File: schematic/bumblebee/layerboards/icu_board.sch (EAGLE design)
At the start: 20 parts, among them P1 B5B-EH-A

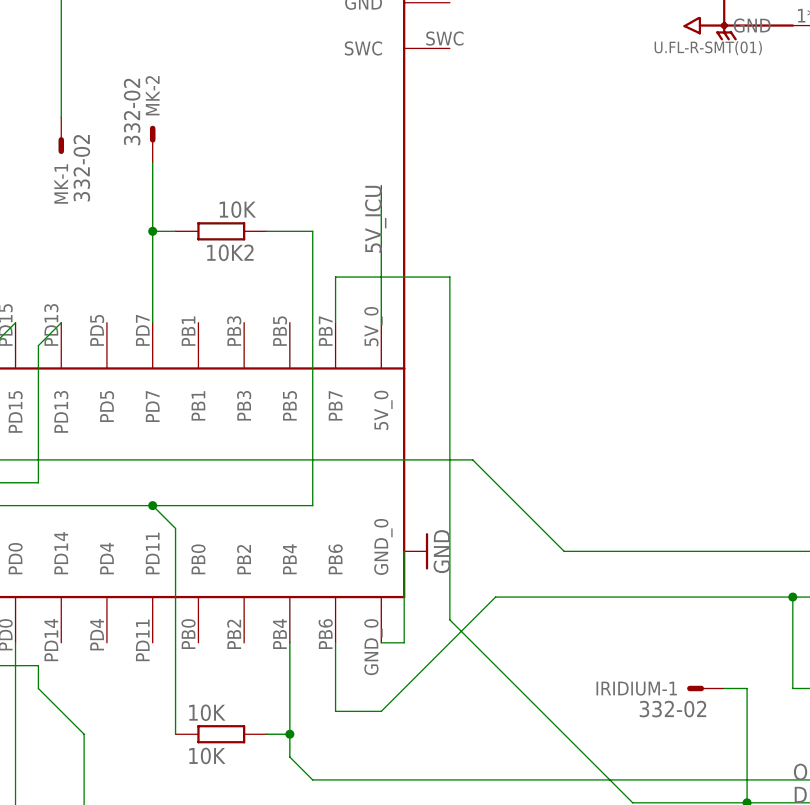
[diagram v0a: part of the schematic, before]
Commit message: CCU и ICU полностью готовы. Было бы здорово, если бы ещё кто-то посмотрел По SCU требуются уточнения
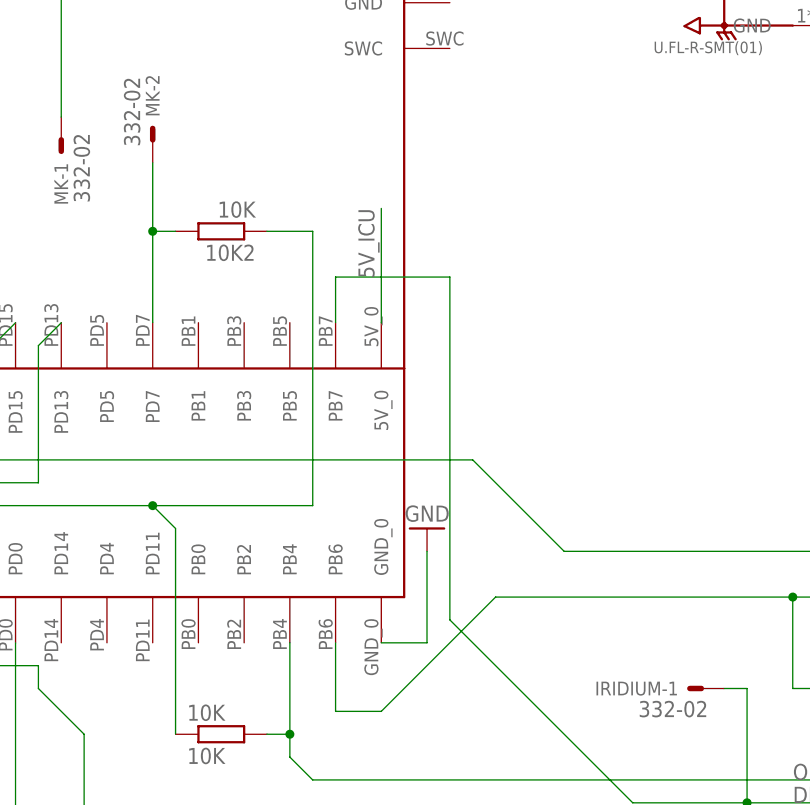
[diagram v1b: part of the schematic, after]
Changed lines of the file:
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@@
 <?xml version="1.0" encoding="utf-8"?>
 <!DOCTYPE eagle SYSTEM "eagle.dtd">
-<eagle version="9.3.2">
+<eagle version="9.3.0">
 <drawing>
 <settings>
@@
 <attribute name="VALUE" x="-38.1" y="109.22" size="1.778" layer="96" rot="R90"/>
 </instance>
-<instance part="GND16" gate="1" x="55.88" y="81.28" smashed="yes" rot="R90">
-<attribute name="VALUE" x="58.42" y="78.74" size="1.778" layer="96" rot="R90"/>
+<instance part="GND16" gate="1" x="55.88" y="83.82" smashed="yes" rot="R180">
+<attribute name="VALUE" x="58.42" y="86.36" size="1.778" layer="96" rot="R180"/>
 </instance>
 </instances>
@@
 <segment>
 <pinref part="U$4" gate="G$1" pin="5V_0"/>
-<wire x1="50.8" y1="106.68" x2="50.8" y2="121.92" width="0.1524" layer="91"/>
-<label x="50.8" y="114.3" size="1.778" layer="95" rot="R90"/>
+<wire x1="50.8" y1="106.68" x2="50.8" y2="119.38" width="0.1524" layer="91"/>
+<label x="48.26" y="119.38" size="1.778" layer="95" rot="R270"/>
 </segment>
 </net>
@@
 <segment>
 <pinref part="U$4" gate="G$1" pin="GND_0"/>
-<wire x1="50.8" y1="71.12" x2="53.34" y2="71.12" width="0.1524" layer="91"/>
-<wire x1="53.34" y1="71.12" x2="53.34" y2="81.28" width="0.1524" layer="91"/>
+<wire x1="50.8" y1="71.12" x2="55.88" y2="71.12" width="0.1524" layer="91"/>
+<wire x1="55.88" y1="71.12" x2="55.88" y2="81.28" width="0.1524" layer="91"/>
 <pinref part="GND16" gate="1" pin="GND"/>
 </segment>

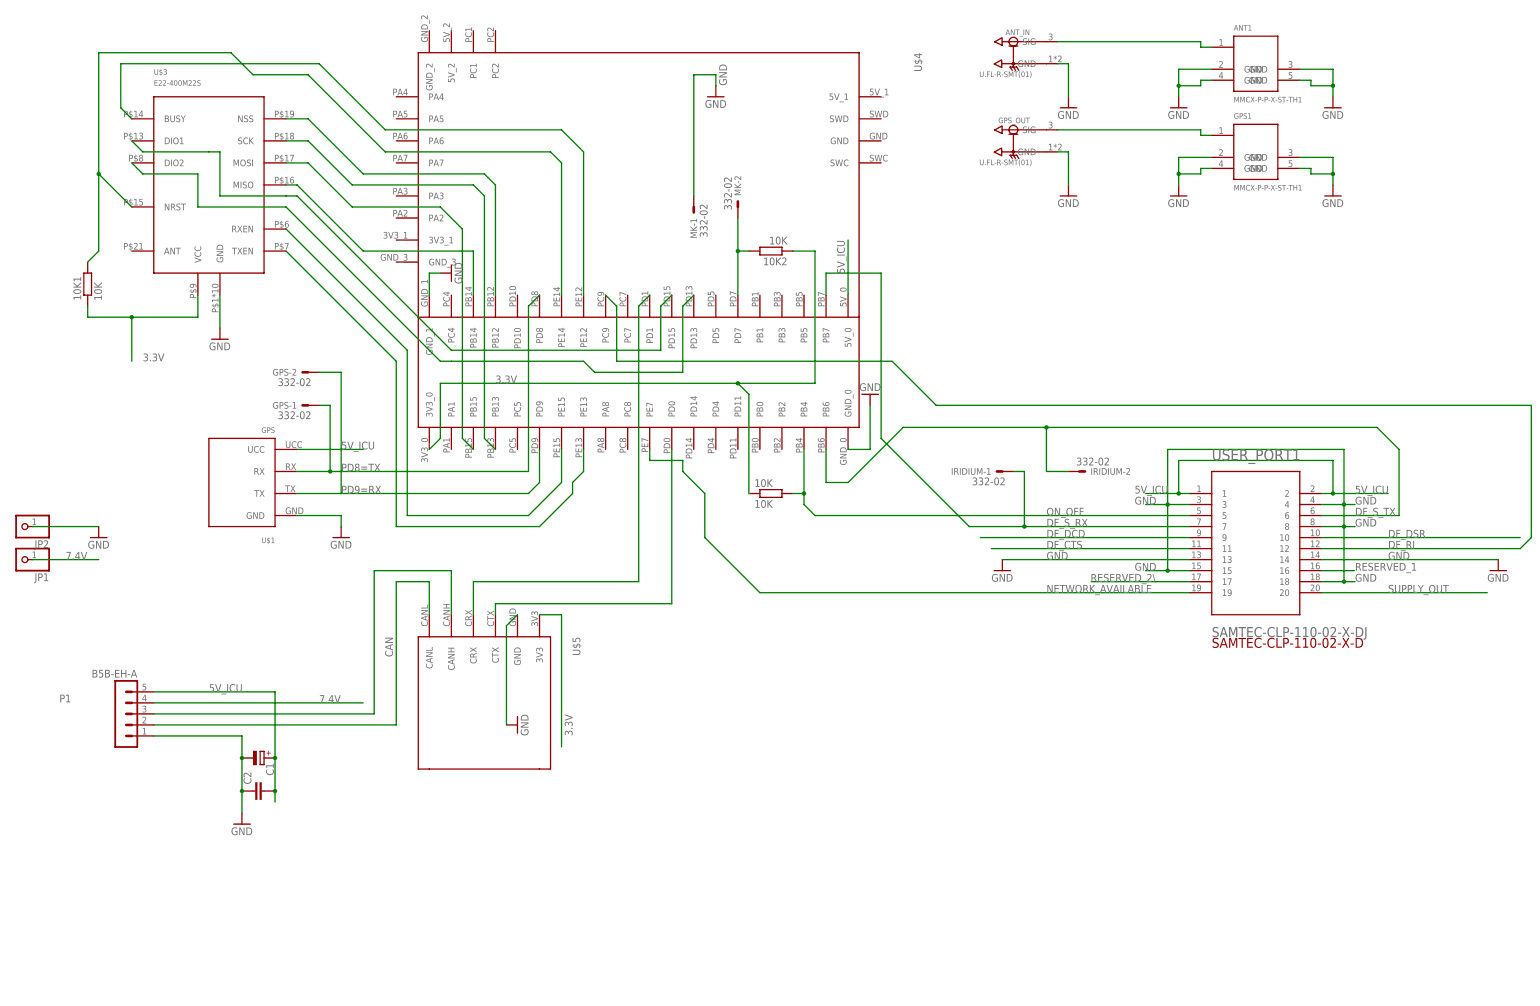
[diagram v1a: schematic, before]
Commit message: ICU готова, SCU скоро доделаю, пока что там всё не очень В либу добавлен LSM303C
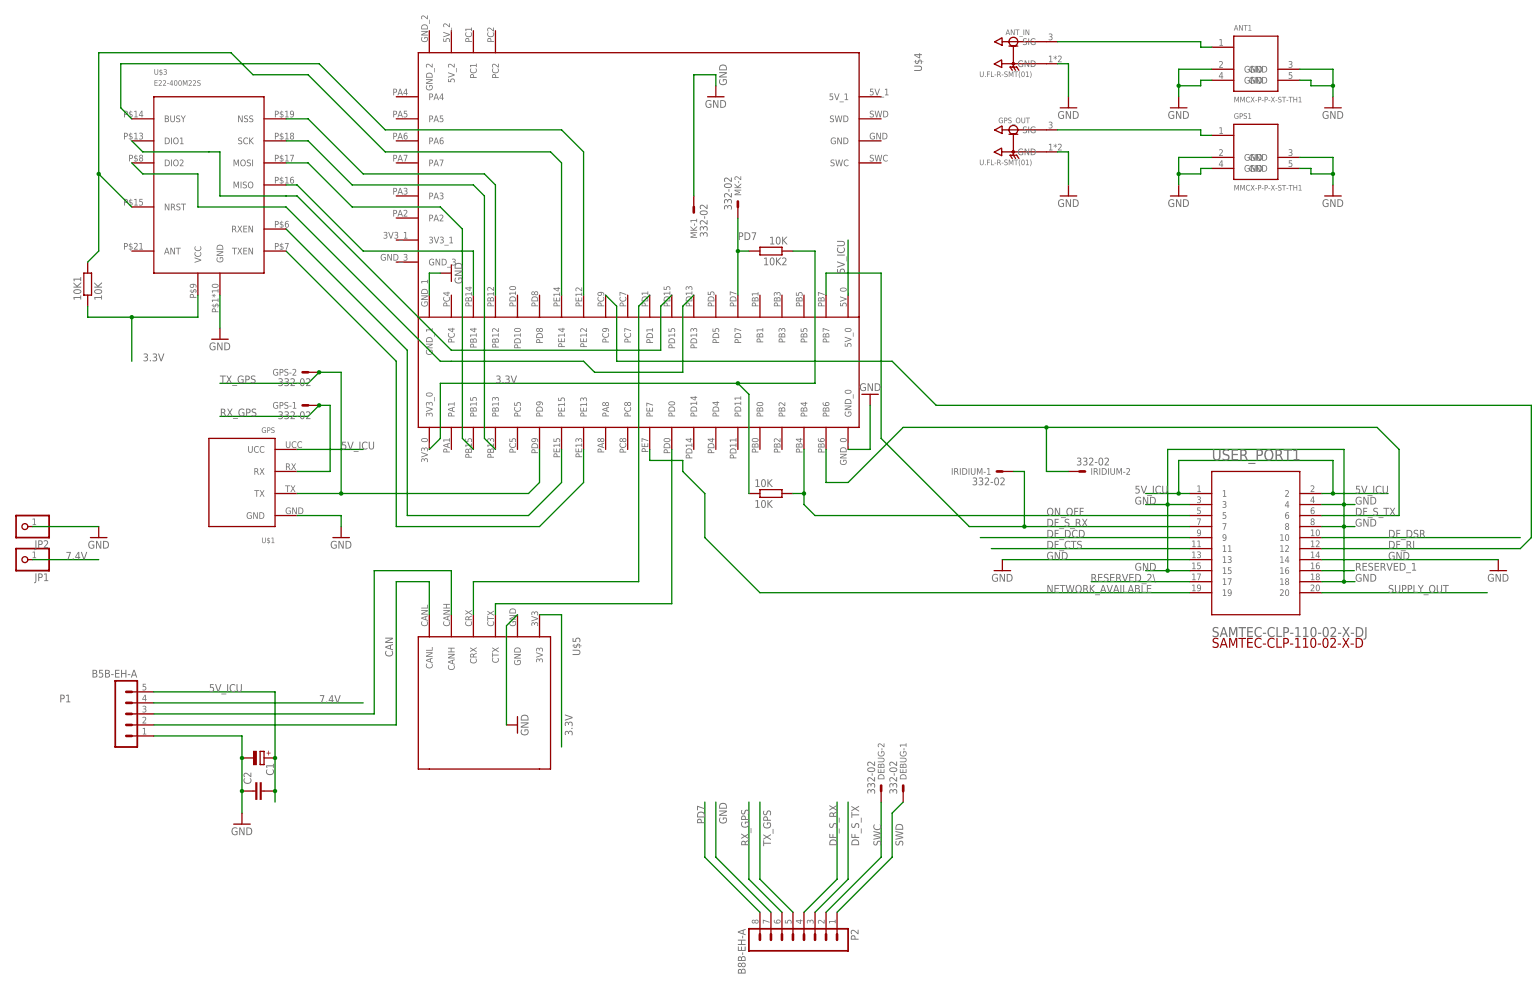
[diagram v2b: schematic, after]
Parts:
- added DEBUG: 332-02, con-garry:332-02
- added P2: B8B-EH-A, con-jst-eh:B8B-EH-A
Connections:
- removed net N$11: 10K2.2, MK-2.S, U$4.PD7
- removed net PD8=TX: GPS-1.S, U$1.RX, U$4.PD8
- removed net PD9=RX: GPS-2.S, U$1.TX, U$4.PD9
- new net PD7: 10K2.2, MK-2.S, P2.8, U$4.PD7
- new net RX_GPS: GPS-1.S, P2.6, U$1.RX
- new net SWC: DEBUG-2.S, P2.2
- new net SWD: DEBUG-1.S, P2.1
- new net TX_GPS: GPS-2.S, P2.5, U$1.TX, U$4.PD9
- net DF_S_RX: now also P2.4
- net DF_S_TX: now also P2.3
- net GND: now also P2.7
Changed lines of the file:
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@@
 <part name="GND15" library="supply1" library_urn="urn:adsk.eagle:library:371" deviceset="GND" device=""/>
 <part name="GND16" library="supply1" library_urn="urn:adsk.eagle:library:371" deviceset="GND" device=""/>
+<part name="DEBUG" library="con-garry" library_urn="urn:adsk.eagle:library:147" deviceset="332-02" device="" package3d_urn="urn:adsk.eagle:package:6810/1"/>
+<part name="P2" library="con-jst-eh" deviceset="B8B-EH-A" device=""/>
 </parts>
 <sheets>
@@
 <instance part="GND16" gate="1" x="55.88" y="83.82" smashed="yes" rot="R180">
 <attribute name="VALUE" x="58.42" y="86.36" size="1.778" layer="96" rot="R180"/>
+</instance>
+<instance part="DEBUG" gate="-1" x="63.5" y="-7.62" smashed="yes" rot="R90">
+<attribute name="NAME" x="64.262" y="-5.08" size="1.524" layer="95" rot="R90"/>
+<attribute name="VALUE" x="62.103" y="-8.382" size="1.778" layer="96" rot="R90"/>
+</instance>
+<instance part="DEBUG" gate="-2" x="58.42" y="-7.62" smashed="yes" rot="R90">
+<attribute name="NAME" x="59.182" y="-5.08" size="1.524" layer="95" rot="R90"/>
+<attribute name="VALUE" x="57.023" y="-8.382" size="1.778" layer="96" rot="R90"/>
+</instance>
+<instance part="P2" gate="G$1" x="38.1" y="-40.64" smashed="yes" rot="R270">
+<attribute name="NAME" x="51.435" y="-39.37" size="1.778" layer="95" rot="R270"/>
+<attribute name="VALUE" x="25.4" y="-39.37" size="1.778" layer="95" rot="R270"/>
 </instance>
 </instances>
@@
 <pinref part="GND16" gate="1" pin="GND"/>
 </segment>
+<segment>
+<pinref part="P2" gate="G$1" pin="7"/>
+<wire x1="33.02" y1="-35.56" x2="20.32" y2="-22.86" width="0.1524" layer="91"/>
+<wire x1="20.32" y1="-22.86" x2="20.32" y2="-10.16" width="0.1524" layer="91"/>
+<label x="22.86" y="-15.24" size="1.778" layer="95" rot="R90"/>
+</segment>
 </net>
 <net name="3.3V" class="0">
@@
 </segment>
 </net>
-<net name="PD8=TX" class="0">
-<segment>
-<pinref part="U$4" gate="G$1" pin="PD8"/>
-<wire x1="-20.32" y1="106.68" x2="-22.86" y2="104.14" width="0.1524" layer="91"/>
-<wire x1="-22.86" y1="104.14" x2="-22.86" y2="66.04" width="0.1524" layer="91"/>
-<pinref part="U$1" gate="G$1" pin="RX"/>
-<wire x1="-22.86" y1="66.04" x2="-68.58" y2="66.04" width="0.1524" layer="91"/>
-<label x="-66.04" y="66.04" size="1.778" layer="95"/>
-<wire x1="-68.58" y1="66.04" x2="-76.2" y2="66.04" width="0.1524" layer="91"/>
-<wire x1="-68.58" y1="66.04" x2="-68.58" y2="81.28" width="0.1524" layer="91"/>
-<wire x1="-68.58" y1="81.28" x2="-71.12" y2="81.28" width="0.1524" layer="91"/>
-<junction x="-68.58" y="66.04"/>
-<pinref part="GPS" gate="-1" pin="S"/>
-</segment>
-</net>
-<net name="PD9=RX" class="0">
+<net name="TX_GPS" class="0">
 <segment>
 <pinref part="U$4" gate="G$1" pin="PD9"/>
@@
 <wire x1="-20.32" y1="63.5" x2="-22.86" y2="60.96" width="0.1524" layer="91"/>
 <wire x1="-22.86" y1="60.96" x2="-66.04" y2="60.96" width="0.1524" layer="91"/>
-<label x="-66.04" y="60.96" size="1.778" layer="95"/>
+<label x="-93.98" y="86.36" size="1.778" layer="95"/>
+<pinref part="GPS" gate="-2" pin="S"/>
 <wire x1="-66.04" y1="60.96" x2="-76.2" y2="60.96" width="0.1524" layer="91"/>
-<wire x1="-66.04" y1="60.96" x2="-66.04" y2="88.9" width="0.1524" layer="91"/>
-<pinref part="GPS" gate="-2" pin="S"/>
 <wire x1="-66.04" y1="88.9" x2="-71.12" y2="88.9" width="0.1524" layer="91"/>
+<wire x1="-66.04" y1="88.9" x2="-66.04" y2="60.96" width="0.1524" layer="91"/>
+<junction x="-66.04" y="60.96"/>
+<wire x1="-71.12" y1="88.9" x2="-73.66" y2="86.36" width="0.1524" layer="91"/>
+<wire x1="-73.66" y1="86.36" x2="-93.98" y2="86.36" width="0.1524" layer="91"/>
+<junction x="-71.12" y="88.9"/>
+</segment>
+<segment>
+<pinref part="P2" gate="G$1" pin="5"/>
+<wire x1="38.1" y1="-35.56" x2="30.48" y2="-27.94" width="0.1524" layer="91"/>
+<wire x1="30.48" y1="-27.94" x2="30.48" y2="-10.16" width="0.1524" layer="91"/>
+<label x="33.02" y="-20.32" size="1.778" layer="95" rot="R90"/>
 </segment>
 </net>
@@
 <wire x1="91.44" y1="66.04" x2="88.9" y2="66.04" width="0.1524" layer="91"/>
 </segment>
+<segment>
+<pinref part="P2" gate="G$1" pin="4"/>
+<wire x1="40.64" y1="-35.56" x2="48.26" y2="-27.94" width="0.1524" layer="91"/>
+<wire x1="48.26" y1="-27.94" x2="48.26" y2="-10.16" width="0.1524" layer="91"/>
+<label x="48.26" y="-20.32" size="1.778" layer="95" rot="R90"/>
+</segment>
 </net>
 <net name="ON_OFF" class="0">
@@
 <wire x1="101.6" y1="66.04" x2="96.52" y2="66.04" width="0.1524" layer="91"/>
 </segment>
+<segment>
+<pinref part="P2" gate="G$1" pin="3"/>
+<wire x1="43.18" y1="-35.56" x2="50.8" y2="-27.94" width="0.1524" layer="91"/>
+<wire x1="50.8" y1="-27.94" x2="50.8" y2="-10.16" width="0.1524" layer="91"/>
+<label x="53.34" y="-20.32" size="1.778" layer="95" rot="R90"/>
+</segment>
 </net>
 <net name="N$6" class="0">
@@
 <pinref part="U$4" gate="G$1" pin="PE15"/>
 <wire x1="-15.24" y1="63.5" x2="-15.24" y2="71.12" width="0.1524" layer="91"/>
-</segment>
-</net>
-<net name="N$7" class="0">
-<segment>
-<pinref part="U$3" gate="G$1" pin="TXEN"/>
-<wire x1="-78.74" y1="116.84" x2="-53.34" y2="91.44" width="0.1524" layer="91"/>
-<wire x1="-53.34" y1="91.44" x2="-53.34" y2="53.34" width="0.1524" layer="91"/>
-<wire x1="-53.34" y1="53.34" x2="-20.32" y2="53.34" width="0.1524" layer="91"/>
-<wire x1="-20.32" y1="53.34" x2="-12.7" y2="60.96" width="0.1524" layer="91"/>
-<wire x1="-12.7" y1="60.96" x2="-12.7" y2="63.5" width="0.1524" layer="91"/>
-<wire x1="-12.7" y1="63.5" x2="-10.16" y2="66.04" width="0.1524" layer="91"/>
-<pinref part="U$4" gate="G$1" pin="PE13"/>
-<wire x1="-10.16" y1="66.04" x2="-10.16" y2="71.12" width="0.1524" layer="91"/>
 </segment>
 </net>
@@
 </segment>
 </net>
-<net name="N$11" class="0">
+<net name="PD7" class="0">
 <segment>
 <pinref part="MK" gate="-2" pin="S"/>
@@
 <wire x1="27.94" y1="116.84" x2="25.4" y2="116.84" width="0.1524" layer="91"/>
 <junction x="25.4" y="116.84"/>
-</segment>
-</net>
+<label x="25.4" y="119.38" size="1.778" layer="95"/>
+</segment>
+<segment>
+<pinref part="P2" gate="G$1" pin="8"/>
+<wire x1="30.48" y1="-35.56" x2="17.78" y2="-22.86" width="0.1524" layer="91"/>
+<wire x1="17.78" y1="-22.86" x2="17.78" y2="-10.16" width="0.1524" layer="91"/>
+<label x="17.78" y="-15.24" size="1.778" layer="95" rot="R90"/>
+</segment>
+</net>
+<net name="RX_GPS" class="0">
+<segment>
+<pinref part="GPS" gate="-1" pin="S"/>
+<wire x1="-68.58" y1="81.28" x2="-71.12" y2="81.28" width="0.1524" layer="91"/>
+<pinref part="U$1" gate="G$1" pin="RX"/>
+<wire x1="-68.58" y1="66.04" x2="-76.2" y2="66.04" width="0.1524" layer="91"/>
+<wire x1="-68.58" y1="66.04" x2="-68.58" y2="81.28" width="0.1524" layer="91"/>
+<label x="-93.98" y="78.74" size="1.778" layer="95"/>
+<wire x1="-71.12" y1="81.28" x2="-73.66" y2="78.74" width="0.1524" layer="91"/>
+<wire x1="-73.66" y1="78.74" x2="-93.98" y2="78.74" width="0.1524" layer="91"/>
+<junction x="-71.12" y="81.28"/>
+</segment>
+<segment>
+<pinref part="P2" gate="G$1" pin="6"/>
+<wire x1="35.56" y1="-35.56" x2="27.94" y2="-27.94" width="0.1524" layer="91"/>
+<wire x1="27.94" y1="-27.94" x2="27.94" y2="-10.16" width="0.1524" layer="91"/>
+<label x="27.94" y="-20.32" size="1.778" layer="95" rot="R90"/>
+</segment>
+</net>
+<net name="N$22" class="0">
+<segment>
+<pinref part="U$4" gate="G$1" pin="PE13"/>
+<wire x1="-10.16" y1="63.5" x2="-10.16" y2="71.12" width="0.1524" layer="91"/>
+<pinref part="U$3" gate="G$1" pin="TXEN"/>
+<wire x1="-78.74" y1="116.84" x2="-53.34" y2="91.44" width="0.1524" layer="91"/>
+<wire x1="-53.34" y1="91.44" x2="-53.34" y2="53.34" width="0.1524" layer="91"/>
+<wire x1="-53.34" y1="53.34" x2="-20.32" y2="53.34" width="0.1524" layer="91"/>
+<wire x1="-20.32" y1="53.34" x2="-10.16" y2="63.5" width="0.1524" layer="91"/>
+</segment>
+</net>
+<net name="SWD" class="0">
+<segment>
+<pinref part="P2" gate="G$1" pin="1"/>
+<wire x1="48.26" y1="-35.56" x2="60.96" y2="-22.86" width="0.1524" layer="91"/>
+<pinref part="DEBUG" gate="-1" pin="S"/>
+<wire x1="60.96" y1="-22.86" x2="60.96" y2="-12.7" width="0.1524" layer="91"/>
+<wire x1="60.96" y1="-12.7" x2="63.5" y2="-10.16" width="0.1524" layer="91"/>
+<label x="63.5" y="-20.32" size="1.778" layer="95" rot="R90"/>
+</segment>
+</net>
+<net name="SWC" class="0">
+<segment>
+<pinref part="P2" gate="G$1" pin="2"/>
+<wire x1="45.72" y1="-35.56" x2="58.42" y2="-22.86" width="0.1524" layer="91"/>
+<wire x1="58.42" y1="-22.86" x2="58.42" y2="-10.16" width="0.1524" layer="91"/>
+<pinref part="DEBUG" gate="-2" pin="S"/>
+<label x="58.42" y="-20.32" size="1.778" layer="95" rot="R90"/>
+</segment>
+</net>

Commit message: Подготовка плат к производству
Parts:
- renumbered GPS to GPS_DBG, JP1 to V7.4, JP2 to GND, MK to TEST_MODE, P1 to FROM_PCU, P2 to DEBUG_OUT, U$1 to GPS_BRD, U$3 to RF, U$4 to GREENBRD, U$5 to CAN

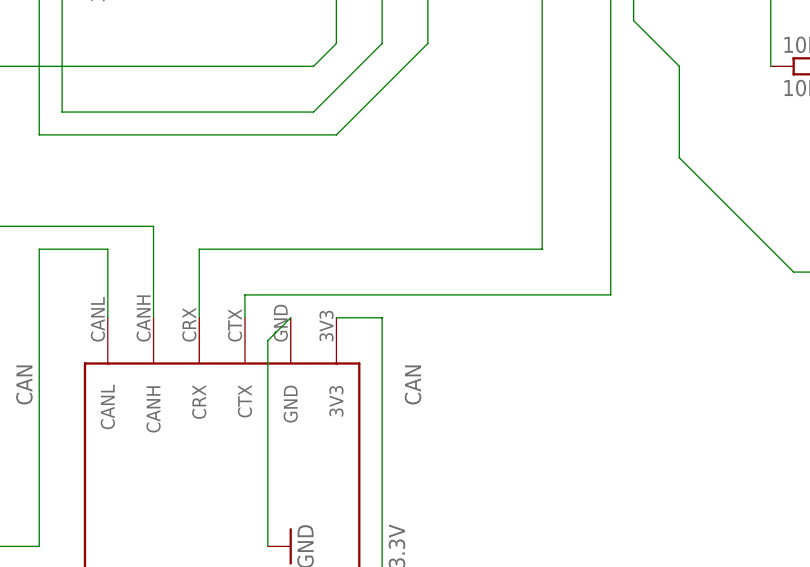
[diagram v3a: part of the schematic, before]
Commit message: Исправил библиотеку Осталось исправить внешнюю плату и сделать плату под антенну GPS
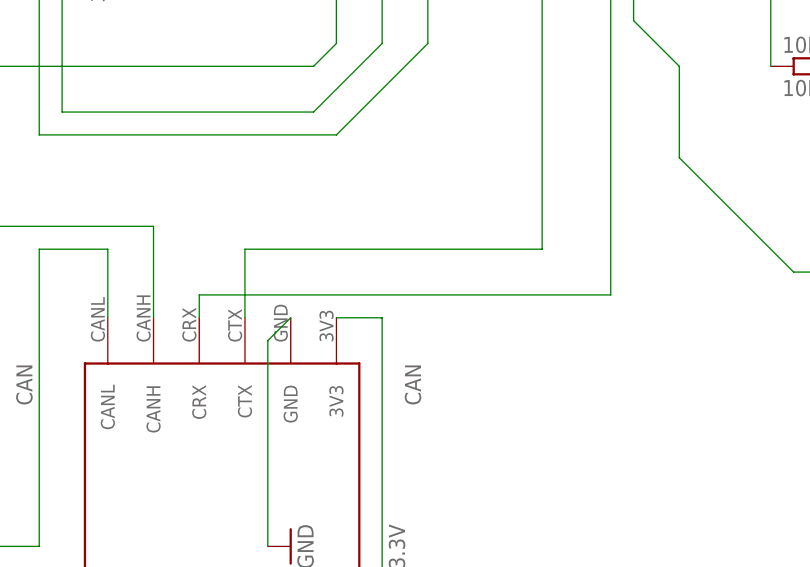
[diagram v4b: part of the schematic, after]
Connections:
- net N$10: now also CAN.CTX; no longer CAN.CRX
- net N$9: now also CAN.CRX; no longer CAN.CTX
